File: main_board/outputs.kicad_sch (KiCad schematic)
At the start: 65 parts, among them J10 3.5mm Jack, J11 3.5mm Jack, J12 3.5mm Jack, J13 3.5mm Jack, J14 3.5mm Jack, J15 3.5mm Jack, J8 3.5mm Jack, J9 3.5mm Jack, U1 TLV2172IDR, U2 TLV2172IDR, U5 TLV2172IDR, U6 LTC1660CGN, U7 LT1790-3.3, U8 TLV2172IDR, U9 TLV2172IDR

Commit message: Ver 2.0 of board.
Also major advances in code.
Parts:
- removed C14: 2.2uF, Capacitor_Tantalum_SMD:CP_EIA-2012-15_AVX-P, symbol Device:CP1_Small
- removed U6: LTC1660CGN, Package_SO:TSSOP-16-1EP_4.4x5mm_P0.65mm, symbol greenface-symbols:LTC1660CGN
- removed U7: LT1790-3.3, Package_TO_SOT_SMD:TSOT-23-6, symbol Reference_Voltage:LT1790-3.3
- added C14: 100nF, Capacitor_SMD:C_0805_2012Metric_Pad1.18x1.45mm_HandSolder, symbol Device:C_Small
- added C31, C43: 330nF, Capacitor_SMD:C_0805_2012Metric_Pad1.18x1.45mm_HandSolder, symbol Device:C_Small
- added Q1: MMBT3904, Package_TO_SOT_SMD:SOT-23, symbol Transistor_BJT:MMBT3904
- added R141: 20K, Resistor_SMD:R_0805_2012Metric_Pad1.20x1.40mm_HandSolder, symbol Device:R_Small_US
- added U15: LM4132xMF-3.3, Package_TO_SOT_SMD:SOT-23-5, symbol Reference_Voltage:LM4132xMF-3.3
- added U6: AD5328, Package_SO:TSSOP-16_4.4x5mm_P0.65mm, symbol greenface:AD5328
- added U7: L78L05_SOT89, Package_TO_SOT_SMD:SOT-89-3, symbol Regulator_Linear:L78L05_SOT89
- C10: value 100nF -> 330nF;  LCSC Part # C49678 -> C107132; Digi-Key Part 478-10836-1-ND -> 311-1888-1-ND
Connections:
- net +3V3 is gone; now on net +12V: C18.1
- net +12V: now also Q1.3 (C), R141.2; no longer C10.1
- net 3.3VRef: now also C14.1, U15.5 (VREF), U6.3 (VDD), U6.8 (REFa_d), U6.9 (REFe_h)
- net A0: now also U6.4 (OUTA)
- net A1: now also U6.5 (OUTB)
- net A2: now also U6.6 (OUTC)
- net A3: now also U6.7 (OUTD)
- net A4: now also U6.10 (OUTE)
- net A5: now also U6.11 (OUTF)
- net A6: now also U6.12 (OUTG)
- net A7: now also U6.13 (OUTH)
- net CLK: now also U6.16 (SCK)
- net CS: now also U6.2 (~{SYNC})
- net DOUT: now also U6.15 (DIN)
- net GND: now also C14.2, C31.2, C43.2, U15.2 (GND), U6.1 (~{LDAC}), U6.14 (GND), U7.2 (GND)
- net Out0: now reaches J8.2 (T), R24.1, U1.1
- net Out1: now reaches J9.2 (T), R25.1, U1.7
- net Out7: now reaches J15.2 (T), R55.1, U9.7
- net Out5: now reaches J13.2 (T), R53.1, U8.7
- net Out2: now reaches J10.2 (T), R26.1, U2.1
- net Out3: now reaches J11.2 (T), R27.1, U2.7
- net Out4: now reaches J12.2 (T), R52.1, U8.1
- net Out6: now reaches J14.2 (T), R54.1, U9.1
- new net: C10.1, U15.4 (VIN), U7.1 (OUT)
- new net: C31.1, Q1.1 (B), R141.1
- new net: C43.1, Q1.2 (E), U7.3 (IN)
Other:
- note removed: "For U6"
- moved on the sheet: C15, C17, C18, J10, J11, J12, J13, J14, J15, J8, J9, R10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

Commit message: Version 0.03
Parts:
- added R142, R143: 100K .1%, Resistor_SMD:R_0805_2012Metric_Pad1.20x1.40mm_HandSolder, symbol Device:R_Small_US
- U1, U2, U8, U9: value TLV2172IDR -> TL072CDR;  LCSC Part # C129149 -> C67473
- U5: value TLV2172IDR -> TL072CDR; footprint Package_SO:SOIC-8-1EP_3.9x4.9mm_P1.27mm_EP2.29x3mm -> Package_SO:SOIC-8_3.9x4.9mm_P1.27mm;  LCSC Part # C129149 -> C67473
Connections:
- net -1.65V: now also R142.2
- net at U5.2 (-): now also R142.1, R143.2; no longer U5.1
- new net +1.65V: R143.1, U5.1
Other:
- moved on the sheet: U5A

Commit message: Version .06
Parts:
- added TP3: TestPoint, TestPoint:TestPoint_Keystone_5005-5009_Compact, symbol Connector:TestPoint
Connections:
- net 3.3VRef: now also TP3.1
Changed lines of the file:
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@@
   (junction (at 217.17 63.5) (diameter 0) (color 0 0 0 0)
   )
+  (junction (at 194.31 19.05) (diameter 0) (color 0 0 0 0)
+  )
   (junction (at 217.17 109.22) (diameter 0) (color 0 0 0 0)
   )
@@
     (stroke (width 0) (type default) (color 0 0 0 0))
   )
+  (wire (pts (xy 22.225 35.56) (xy 48.895 35.56))
+    (stroke (width 0) (type default) (color 0 0 0 0))
+  )
   (wire (pts (xy 123.825 158.75) (xy 123.825 161.925))
     (stroke (width 0) (type default) (color 0 0 0 0))
@@
   )
   (wire (pts (xy 109.22 181.61) (xy 109.22 186.055))
-    (stroke (width 0) (type default) (color 0 0 0 0))
-  )
-  (wire (pts (xy 45.72 35.56) (xy 48.895 35.56))
     (stroke (width 0) (type default) (color 0 0 0 0))
   )
@@
     )
   )
-  (global_label "CS" (shape input) (at 45.72 35.56 180) (fields_autoplaced)
-    (effects (font (size 1.27 1.27)) (justify right))
-    (property "Intersheet References" "${INTERSHEET_REFS}" (id 0) (at 40.9163 35.4806 0)
+  (global_label "CS" (shape input) (at 22.225 35.56 180) (fields_autoplaced)
+    (effects (font (size 1.27 1.27)) (justify right))
+    (property "Intersheet References" "${INTERSHEET_REFS}" (id 0) (at 17.4213 35.4806 0)
       (effects (font (size 1.27 1.27)) (justify right) hide)
     )
@@
     (pin "4")
   )
+  (symbol (lib_id "Connector:TestPoint") (at 194.31 19.05 0) (unit 1)
+    (in_bom yes) (on_board yes)
+    (property "Reference" "TP3" (id 0) (at 195.7832 16.0528 0)
+      (effects (font (size 1.27 1.27)) (justify left))
+    )
+    (property "Value" "TestPoint" (id 1) (at 195.7832 18.3642 0)
+      (effects (font (size 1.27 1.27)) (justify left) hide)
+    )
+    (property "Footprint" "TestPoint:TestPoint_Keystone_5005-5009_Compact" (id 2) (at 199.39 19.05 0)
+      (effects (font (size 1.27 1.27)) hide)
+    )
+    (property "Datasheet" "~" (id 3) (at 199.39 19.05 0)
+      (effects (font (size 1.27 1.27)) hide)
+    )
+    (property "Digi-Key Part" "36-5006-ND" (id 4) (at 194.31 19.05 0)
+      (effects (font (size 1.27 1.27)) hide)
+    )
+    (pin "1")
+  )
   (symbol (lib_id "Device:R_Small_US") (at 207.645 133.35 270) (unit 1)

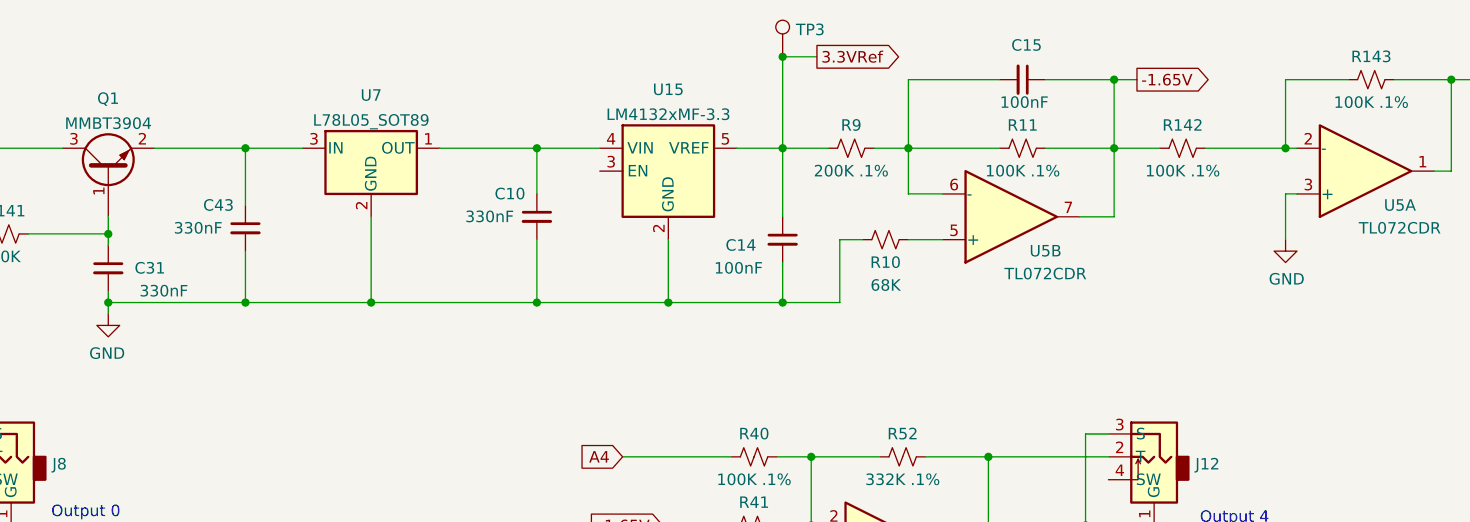
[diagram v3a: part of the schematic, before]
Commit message: Updates monitor circuitry. Sets outputs on init().
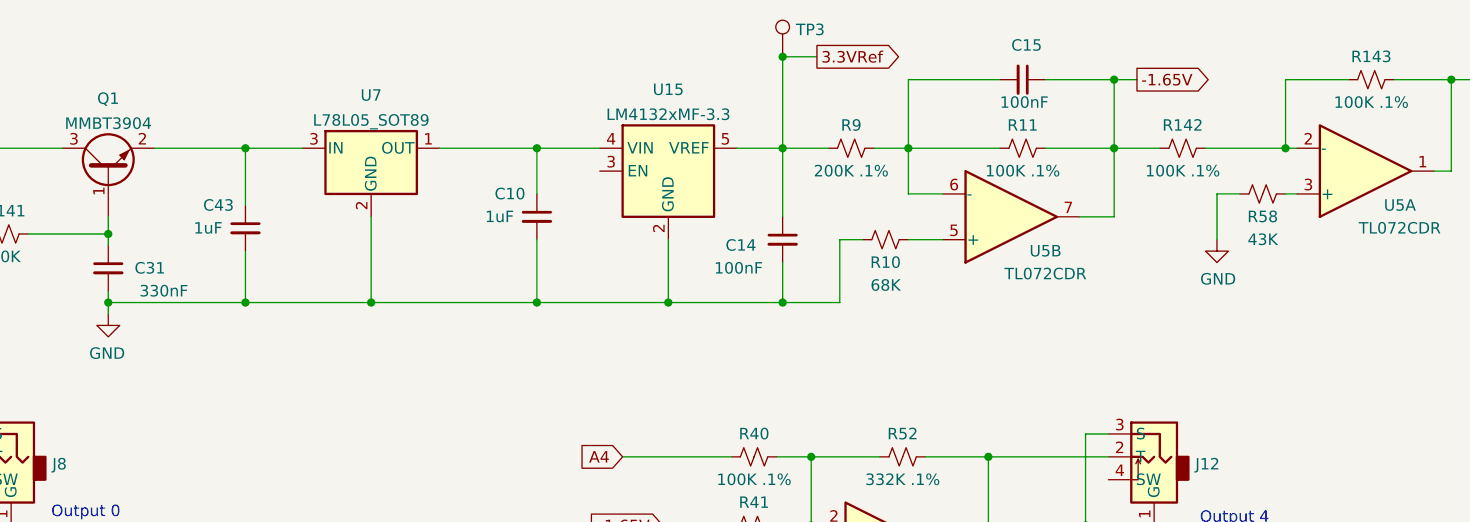
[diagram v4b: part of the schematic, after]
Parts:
- added R58: 43K, Resistor_SMD:R_0805_2012Metric_Pad1.20x1.40mm_HandSolder, symbol Device:R_Small_US
- C10, C43: value 330nF -> 1uF;  LCSC Part # C107132 -> C28323
- C31:  LCSC Part # C107132 -> C1740
- R10:  LCSC Part # C137412 -> C17801
- R141:  LCSC Part # C237133 -> C4328
- R20, R21, R22, R23, R48, R49, R50, R51:  LCSC Part # C137429 -> C17695
- U1, U2, U5, U8, U9:  LCSC Part # C67473 -> C6961
- U7:  LCSC Part # C90471 -> C71136
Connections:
- net GND: now also R58.2; no longer U5.3 (+)
- new net: R58.1, U5.3 (+)

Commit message: Upgrades board to v5. Adds Bonk Daddy.
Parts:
- added C23, C29: 100nF, Capacitor_SMD:C_0805_2012Metric_Pad1.18x1.45mm_HandSolder, symbol Device:C_Small
- added C44, C45, C46, C47, C48, C49, C50, C51: 10nF, Capacitor_SMD:C_0805_2012Metric_Pad1.18x1.45mm_HandSolder, symbol Device:C_Small
- added D43, D44: 7.5V, Diode_SMD:D_SOD-123, symbol Device:D_Zener_Small
- added R59, R60: 680, Resistor_SMD:R_0805_2012Metric_Pad1.20x1.40mm_HandSolder, symbol Device:R_Small_US
- added R61, R62, R63, R64, R65, R73, R74, R75: 100K .1%, Resistor_SMD:R_0805_2012Metric_Pad1.20x1.40mm_HandSolder, symbol Device:R_Small_US
- added U13, U24: DG412xY, Package_SO:SOIC-16_3.9x9.9mm_P1.27mm, symbol Analog_Switch:DG412xY
- added U21: MCP23008-xSS, Package_SO:SSOP-20_5.3x7.2mm_P0.65mm, symbol Interface_Expansion:MCP23008-xSS
- TP3: footprint TestPoint:TestPoint_Keystone_5005-5009_Compact -> TestPoint:TestPoint_Keystone_5000-5004_Miniature;  LCSC Part # (none) -> C238123; Digi-Key Part 36-5006-ND -> 36-5002-ND
- U2, U8: footprint Package_SO:SOIC-8-1EP_3.9x4.9mm_P1.27mm_EP2.29x3mm -> Package_SO:SOIC-8_3.9x4.9mm_P1.27mm
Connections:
- net +12V: now also R59.1
- net -1.65V: now also U13.10, U13.15, U13.2, U13.6, U24.10, U24.15, U24.2, U24.6
- net -12V: now also R60.1
- net GND: now also C23.2, C29.1, C44.2, C45.2, C46.2, C47.2, C48.2, C49.2, C50.2, C51.2, D43.2 (A), D44.1 (K), U13.5 (GND), U21.3 (A2), U21.4 (A1), U21.5 (A0), U21.9 (VSS), U24.5 (GND)
- net at R12.1, R13.1, R24.2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: now also R61.1
- net at R46.1, R47.1, R55.2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: now also R75.1
- net at R14.1, R15.1, R25.2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: now also R62.1
- net at R42.1, R43.1, R53.2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: now also R73.1
- net at R16.1, R17.1, R26.2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: now also R63.1
- net at R44.1, R45.1, R54.2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: now also R74.1
- net at R18.1, R19.1, R27.2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: now also R64.1
- net at R40.1, R41.1, R52.2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: now also R65.1
- new net: C48.1, R65.2, U24.3
- new net: C50.1, R74.2, U24.11
- new net: C46.1, R63.2, U13.11
- new net: C45.1, R62.2, U13.7
- new net: C44.1, R61.2, U13.3
- new net: C47.1, R64.2, U13.14
- new net: C51.1, R75.2, U24.14
- new net: C49.1, R73.2, U24.7
- new net +3V3: U13.12 (VL), U21.20 (VDD), U24.12 (VL)
- new net +7.5V: C23.1, D43.1 (K), R59.2, U13.13 (V+), U24.13 (V+)
- new net -7.5V: C29.2, D44.2 (A), R60.2, U13.4 (V-), U24.4 (V-)
- new net G0: U13.1, U21.12 (GP0)
- new net G1: U13.8, U21.13 (GP1)
- new net G2: U13.9, U21.14 (GP2)
- new net G3: U13.16, U21.15 (GP3)
- new net G4: U21.16 (GP4), U24.1
- new net G5: U21.17 (GP5), U24.8
- new net G6: U21.18 (GP6), U24.9
- new net G7: U21.19 (GP7), U24.16
- new net Reset: U21.6 (~{RESET})
- new net SCL: U21.1 (SCL)
- new net SDA: U21.2 (SDA)
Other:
- moved on the sheet: C18, C19, C20, C21, C22, C3, C4, C5, C6, C8, C9, J10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

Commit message: Adds 2HP BonkDaddy. Fixes boms/cpl. Updates Readme
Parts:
- R9:  LCSC Part # C473320 -> C332260
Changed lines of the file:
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@@
   (symbol (lib_id "power:GND") (at 25.4 99.695 0) (mirror y) (unit 1)
     (in_bom yes) (on_board yes)
-    (property "Reference" "#PWR?" (id 0) (at 25.4 106.045 0)
+    (property "Reference" "#PWR0121" (id 0) (at 25.4 106.045 0)
       (effects (font (size 1.27 1.27)) hide)
     )
@@
       (effects (font (size 1.27 1.27)) hide)
     )
-    (property " LCSC Part #" "C473320" (id 5) (at 201.93 29.21 0)
-      (effects (font (size 1.27 1.27)) hide)
-    )
+    (property " LCSC Part #" "C332260" (id 5) (at 201.93 29.21 0)
+      (effects (font (size 1.27 1.27)) hide)
+    )

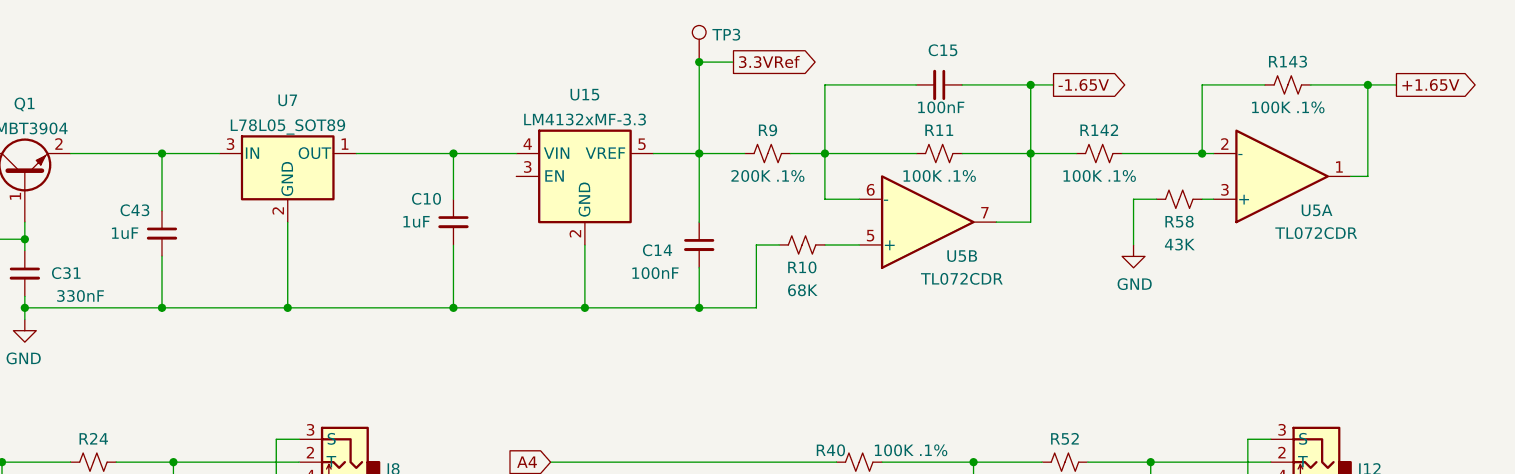
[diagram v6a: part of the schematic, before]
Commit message: Updates main_board, uses generate_boms.bat
Updates reverse protection circuitry on main board.
Updates 3.3V reference circuitry.
Uses generate_boms and retires .xlsx BOM files.
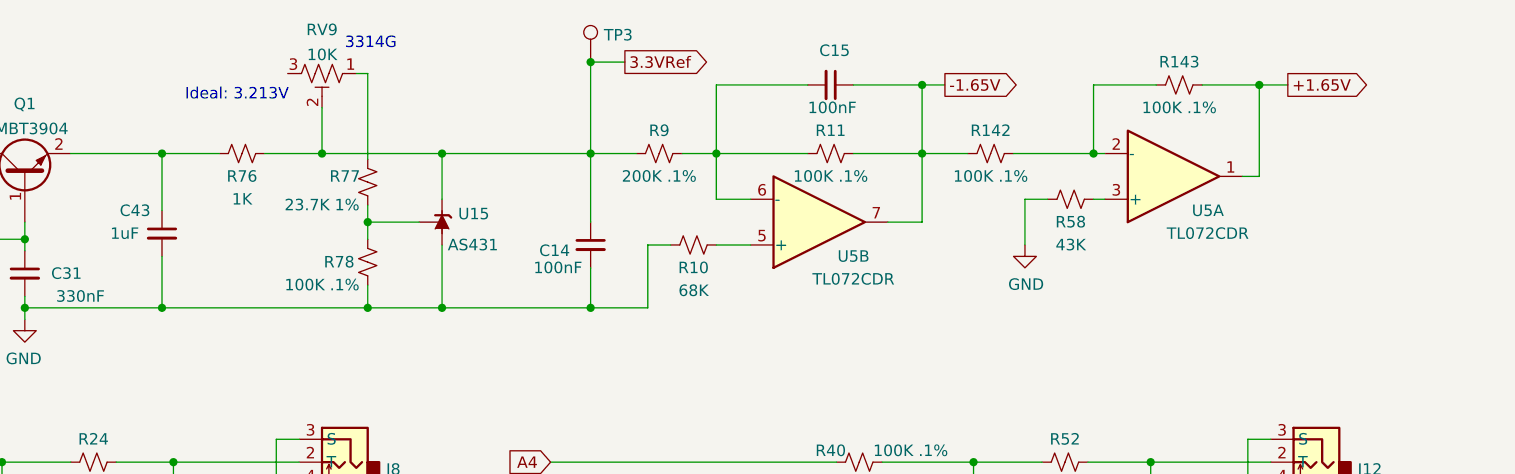
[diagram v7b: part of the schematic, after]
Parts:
- removed C10: 1uF, Capacitor_SMD:C_0805_2012Metric_Pad1.18x1.45mm_HandSolder, symbol Device:C_Small
- removed U15: LM4132xMF-3.3, Package_TO_SOT_SMD:SOT-23-5, symbol Reference_Voltage:LM4132xMF-3.3
- removed U7: L78L05_SOT89, Package_TO_SOT_SMD:SOT-89-3, symbol Regulator_Linear:L78L05_SOT89
- added R76: 1K, Resistor_SMD:R_0603_1608Metric, symbol Device:R_Small_US
- added R77: 23.7K 1%, Resistor_SMD:R_0603_1608Metric, symbol Device:R_Small_US
- added R78: 100K .1%, Resistor_SMD:R_0805_2012Metric_Pad1.20x1.40mm_HandSolder, symbol Device:R_Small_US
- added RV9: 10K, sputterizer:Potentiometer_Bourns_3224W_Vertical, symbol Device:R_Potentiometer_Trim_US
- added U15: AS431, Package_TO_SOT_SMD:SOT-23, symbol Reference_Voltage:TL431DBZ
- C14, C15, C17, C18, C19, C20, C21, C22, C23, C29, C3, C4, C5, C6, C8, C9:  LCSC Part # C49678 -> (none); LCSC Part # (none) -> C49678
- C31:  LCSC Part # C1740 -> (none); LCSC Part # (none) -> C1740
- C43:  LCSC Part # C28323 -> (none); LCSC Part # (none) -> C28323
- C44, C45, C46, C47, C48, C49, C50, C51:  LCSC Part # C1710 -> (none); LCSC Part # (none) -> C1710
- D43, D44:  LCSC Part # C545306 -> (none); LCSC Part # (none) -> C545306
- Q1:  LCSC Part # C94514 -> (none); LCSC Part # (none) -> C94514
- R10:  LCSC Part # C17801 -> (none); LCSC Part # (none) -> C17801
- R11, R12, R13, R14, R142, R143, R15, R16, R17, R18, R19, R40, R41, R42, R43, R44, R45, R46, R47, R61, R62, R63, R64, R65, R73, R74, R75:  LCSC Part # C122537 -> (none); LCSC Part # (none) -> C122537
- R141:  LCSC Part # C4328 -> (none); LCSC Part # (none) -> C4328
- R20, R21, R22, R23, R48, R49, R50, R51, R58:  LCSC Part # C17695 -> (none); LCSC Part # (none) -> C17695
- R24, R25, R26, R27, R52, R53, R54, R55:  LCSC Part # C228750 -> (none); LCSC Part # (none) -> C228750
- R59, R60:  LCSC Part # C17798 -> (none); LCSC Part # (none) -> C17798
- R9:  LCSC Part # C332260 -> (none); LCSC Part # (none) -> C332260
- TP3:  LCSC Part # C238123 -> (none); LCSC Part # (none) -> C238123
- U1, U2, U5, U8, U9:  LCSC Part # C6961 -> (none); LCSC Part # (none) -> C6961
- U13, U24:  LCSC Part # C143730 -> (none); LCSC Part # (none) -> C143730
- U21:  LCSC Part # C148011 -> (none); LCSC Part # (none) -> C148011
- U6:  LCSC Part # C29162 -> (none); LCSC Part # (none) -> C29162
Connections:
- net 3.3VRef: now also R76.1, RV9.2, U15.1 (K)
- net GND: now also R78.2, U15.3 (A)
- net at C43.1, Q1.2 (E): now also R76.2
- new net: R77.1, R78.1, U15.2 (REF)
- new net: R77.2, RV9.1
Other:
- note added: "3314G"
- note added: "Ideal: 3.213V"
- moved on the sheet: C14, C15, R10, R11, R142, R143, R58, R9, TP3, U5A, U5B
